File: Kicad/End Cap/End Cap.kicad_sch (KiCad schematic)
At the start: 12 parts, among them J1 1.27mm 4 pin header, J2 Keystone 3579, J3 Keystone 3569, J4 Keystone 3579, J5 Keystone 3569, J6 Keystone 3579, J7 Keystone 3569, J8 Keystone 3579, J9 Keystone 3569

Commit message: Exported 3D model for End Cap
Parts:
- J3, J5, J7, J9: footprint custom_Connector:Keystone_3569 -> custom_Connector:Keystone_3569_half
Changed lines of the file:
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@@
 			)
 		)
-		(property "Footprint" "custom_Connector:Keystone_3569"
+		(property "Footprint" "custom_Connector:Keystone_3569_half"
 			(at 129.54 153.67 0)
 			(effects
@@
 			)
 		)
-		(property "Footprint" "custom_Connector:Keystone_3569"
+		(property "Footprint" "custom_Connector:Keystone_3569_half"
 			(at 129.54 121.92 0)
 			(effects
@@
 			)
 		)
-		(property "Footprint" "custom_Connector:Keystone_3569"
+		(property "Footprint" "custom_Connector:Keystone_3569_half"
 			(at 129.54 163.83 0)
 			(effects
@@
 			)
 		)
-		(property "Footprint" "custom_Connector:Keystone_3569"
+		(property "Footprint" "custom_Connector:Keystone_3569_half"
 			(at 129.54 111.76 0)
 			(effects

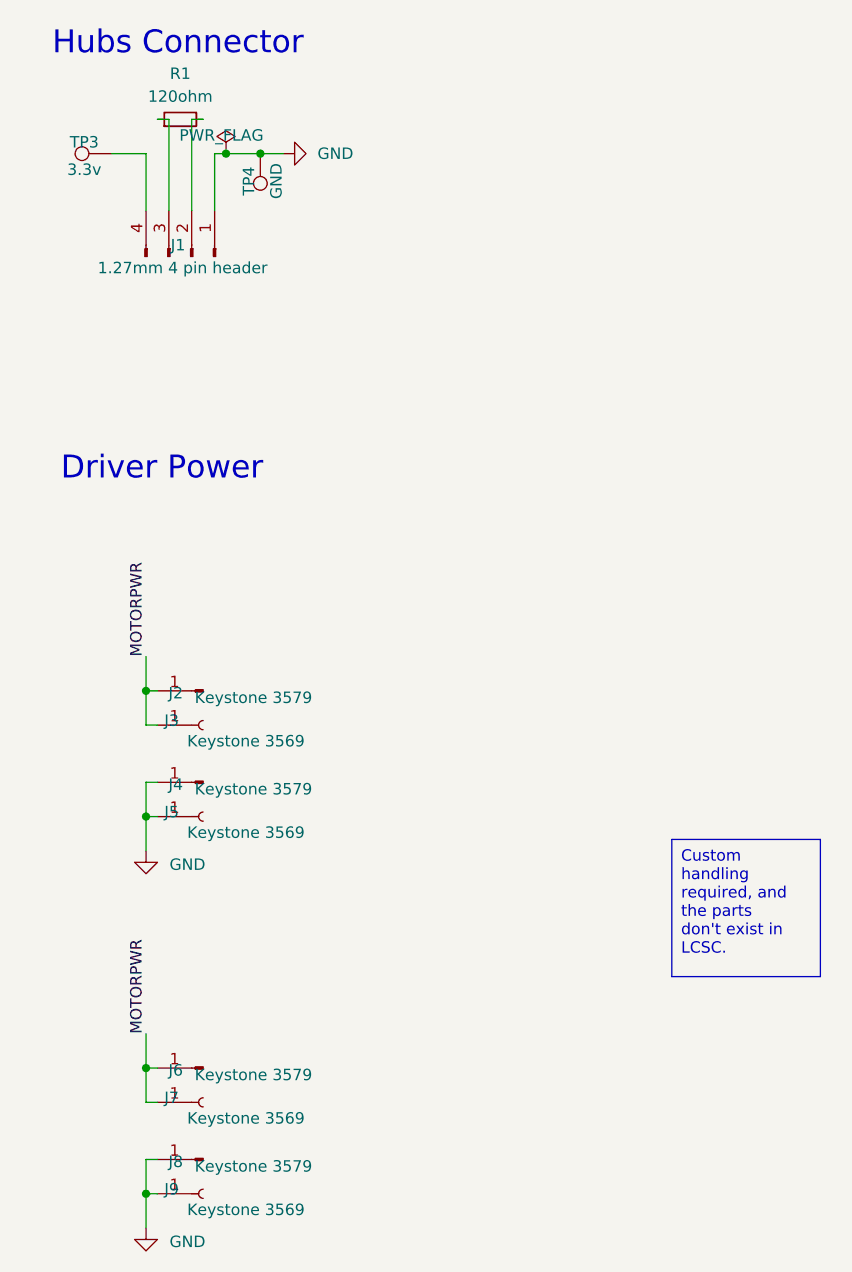
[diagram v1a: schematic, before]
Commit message: Added LCSC part numbers, DNP attr, and exported Gerbers
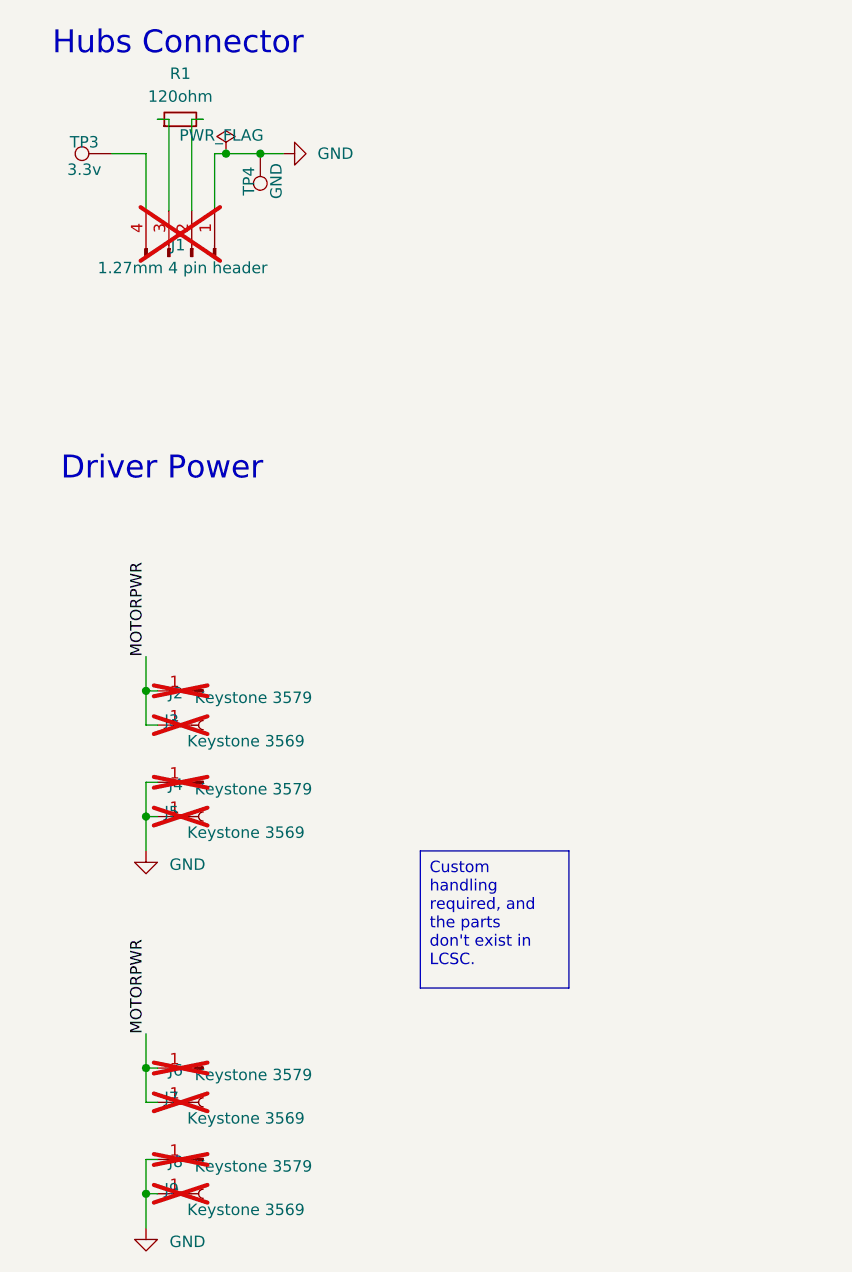
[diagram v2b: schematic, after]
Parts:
- J1, J2, J3, J4, J5, J6, J7, J8, J9: now not fitted
- R1: LCSC (none) -> C25079
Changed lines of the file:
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@@
 	(text_box "Custom handling required, and the parts don't exist in LCSC."
 		(exclude_from_sim no)
-		(at 181.61 124.46 0)
+		(at 153.67 125.73 0)
 		(size 16.51 15.24)
 		(stroke
@@
 		(in_bom yes)
 		(on_board yes)
-		(dnp no)
+		(dnp yes)
 		(property "Reference" "J7"
 			(at 125.222 153.162 0)
@@
 		(in_bom yes)
 		(on_board yes)
-		(dnp no)
+		(dnp yes)
 		(property "Reference" "J8"
 			(at 126.492 160.274 0)
@@
 		(in_bom yes)
 		(on_board yes)
-		(dnp no)
+		(dnp yes)
 		(property "Reference" "J5"
 			(at 125.222 121.412 0)
@@
 		(in_bom yes)
 		(on_board yes)
-		(dnp no)
+		(dnp yes)
 		(property "Reference" "J1"
 			(at 126.746 58.42 90)
@@
 		(in_bom yes)
 		(on_board yes)
-		(dnp no)
+		(dnp yes)
 		(property "Reference" "J9"
 			(at 125.222 163.322 0)
@@
 		(in_bom yes)
 		(on_board yes)
-		(dnp no)
+		(dnp yes)
 		(property "Reference" "J4"
 			(at 126.492 118.364 0)
@@
 			)
 		)
+		(property "LCSC" "C25079"
+			(at 127 39.37 0)
+			(effects
+				(font
+					(size 1.27 1.27)
+				)
+				(hide yes)
+			)
+		)
 		(pin "1"
 		)
@@
 		(in_bom yes)
 		(on_board yes)
-		(dnp no)
+		(dnp yes)
 		(property "Reference" "J3"
 			(at 125.222 111.252 0)
@@
 		(in_bom yes)
 		(on_board yes)
-		(dnp no)
+		(dnp yes)
 		(property "Reference" "J6"
 			(at 126.492 150.114 0)
@@
 		(in_bom yes)
 		(on_board yes)
-		(dnp no)
+		(dnp yes)
 		(property "Reference" "J2"
 			(at 126.492 108.204 0)
